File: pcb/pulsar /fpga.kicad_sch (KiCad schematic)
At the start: 0 parts

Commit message: feat(pcb): FPGA A1 schematic complete — MGT, ADC0-7 pinout, MUX sel
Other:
- added sheet A1 (MGT, clock) (fpga_a1.kicad_sch)
- added sheet B2 (IO bank 1) (fpga_b2.kicad_sch)
- added sheet C3 (IO bank 2) (fpga_c3.kicad_sch)
- added sheet D4 (IO bank 3) (fpga_d4.kicad_sch .kicad_sch)
- added sheet E5 (power + config) (fpga_e5.kicad_sch)
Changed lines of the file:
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@@
 	(generator_version "10.0")
 	(paper "A4")
+	(sheet
+		(at 114.3 73.66)
+		(size 90.17 40.64)
+		(exclude_from_sim no)
+		(in_bom yes)
+		(on_board yes)
+		(dnp no)
+		(fields_autoplaced yes)
+		(stroke
+			(width 0.1524)
+			(type solid)
+		)
+		(fill
+			(color 0 0 0 0)
+		)
+		(property "Sheetname" "D4 (IO bank 3)"
+			(at 114.3 72.9484 0)
+			(show_name no)
+			(do_not_autoplace no)
+			(effects
+				(font
+					(size 1.27 1.27)
+				)
+				(justify left bottom)
+			)
+		)
+		(property "Sheetfile" "fpga_d4.kicad_sch .kicad_sch"
+			(at 114.3 114.8846 0)
+			(show_name no)
+			(do_not_autoplace no)
+			(effects
+				(font
+					(size 1.27 1.27)
+				)
+				(justify left top)
+			)
+		)
+		(instances
+			(project "pulsar "
+				(path "/60c284f0-e6d7-47fc-9b46-38b478ecbf26/80956d0d-0521-4a41-bffb-11a8f02bc21e"
+					(page "11")
+				)
+			)
+		)
+	)
+	(sheet
+		(at 26.67 73.66)
+		(size 80.01 40.64)
+		(exclude_from_sim no)
+		(in_bom yes)
+		(on_board yes)
+		(dnp no)
+		(fields_autoplaced yes)
+		(stroke
+			(width 0.1524)
+			(type solid)
+		)
+		(fill
+			(color 0 0 0 0)
+		)
+		(property "Sheetname" "C3 (IO bank 2)"
+			(at 26.67 72.9484 0)
+			(show_name no)
+			(do_not_autoplace no)
+			(effects
+				(font
+					(size 1.27 1.27)
+				)
+				(justify left bottom)
+			)
+		)
+		(property "Sheetfile" "fpga_c3.kicad_sch"
+			(at 26.67 114.8846 0)
+			(show_name no)
+			(do_not_autoplace no)
+			(effects
+				(font
+					(size 1.27 1.27)
+				)
+				(justify left top)
+			)
+		)
+		(instances
+			(project "pulsar "
+				(path "/60c284f0-e6d7-47fc-9b46-38b478ecbf26/80956d0d-0521-4a41-bffb-11a8f02bc21e"
+					(page "10")
+				)
+			)
+		)
+	)
+	(sheet
+		(at 26.67 123.19)
+		(size 80.01 43.18)
+		(exclude_from_sim no)
+		(in_bom yes)
+		(on_board yes)
+		(dnp no)
+		(fields_autoplaced yes)
+		(stroke
+			(width 0.1524)
+			(type solid)
+		)
+		(fill
+			(color 0 0 0 0)
+		)
+		(property "Sheetname" "E5 (power + config)"
+			(at 26.67 122.4784 0)
+			(show_name no)
+			(do_not_autoplace no)
+			(effects
+				(font
+					(size 1.27 1.27)
+				)
+				(justify left bottom)
+			)
+		)
+		(property "Sheetfile" "fpga_e5.kicad_sch"
+			(at 26.67 166.9546 0)
+			(show_name no)
+			(do_not_autoplace no)
+			(effects
+				(font
+					(size 1.27 1.27)
+				)
+				(justify left top)
+			)
+		)
+		(instances
+			(project "pulsar "
+				(path "/60c284f0-e6d7-47fc-9b46-38b478ecbf26/80956d0d-0521-4a41-bffb-11a8f02bc21e"
+					(page "12")
+				)
+			)
+		)
+	)
+	(sheet
+		(at 114.3 21.59)
+		(size 90.17 46.99)
+		(exclude_from_sim no)
+		(in_bom yes)
+		(on_board yes)
+		(dnp no)
+		(fields_autoplaced yes)
+		(stroke
+			(width 0.1524)
+			(type solid)
+		)
+		(fill
+			(color 0 0 0 0)
+		)
+		(property "Sheetname" "B2 (IO bank 1)"
+			(at 114.3 20.8784 0)
+			(show_name no)
+			(do_not_autoplace no)
+			(effects
+				(font
+					(size 1.27 1.27)
+				)
+				(justify left bottom)
+			)
+		)
+		(property "Sheetfile" "fpga_b2.kicad_sch"
+			(at 114.3 69.1646 0)
+			(show_name no)
+			(do_not_autoplace no)
+			(effects
+				(font
+					(size 1.27 1.27)
+				)
+				(justify left top)
+			)
+		)
+		(instances
+			(project "pulsar "
+				(path "/60c284f0-e6d7-47fc-9b46-38b478ecbf26/80956d0d-0521-4a41-bffb-11a8f02bc21e"
+					(page "9")
+				)
+			)
+		)
+	)
+	(sheet
+		(at 26.67 21.59)
+		(size 80.01 46.99)
+		(exclude_from_sim no)
+		(in_bom yes)
+		(on_board yes)
+		(dnp no)
+		(fields_autoplaced yes)
+		(stroke
+			(width 0.1524)
+			(type solid)
+		)
+		(fill
+			(color 0 0 0 0)
+		)
+		(property "Sheetname" "A1 (MGT, clock)"
+			(at 26.67 20.8784 0)
+			(show_name no)
+			(do_not_autoplace no)
+			(effects
+				(font
+					(size 1.27 1.27)
+				)
+				(justify left bottom)
+			)
+		)
+		(property "Sheetfile" "fpga_a1.kicad_sch"
+			(at 26.67 69.1646 0)
+			(show_name no)
+			(do_not_autoplace no)
+			(effects
+				(font
+					(size 1.27 1.27)
+				)
+				(justify left top)
+			)
+		)
+		(instances
+			(project "pulsar "
+				(path "/60c284f0-e6d7-47fc-9b46-38b478ecbf26/80956d0d-0521-4a41-bffb-11a8f02bc21e"
+					(page "8")
+				)
+			)
+		)
+	)
 )

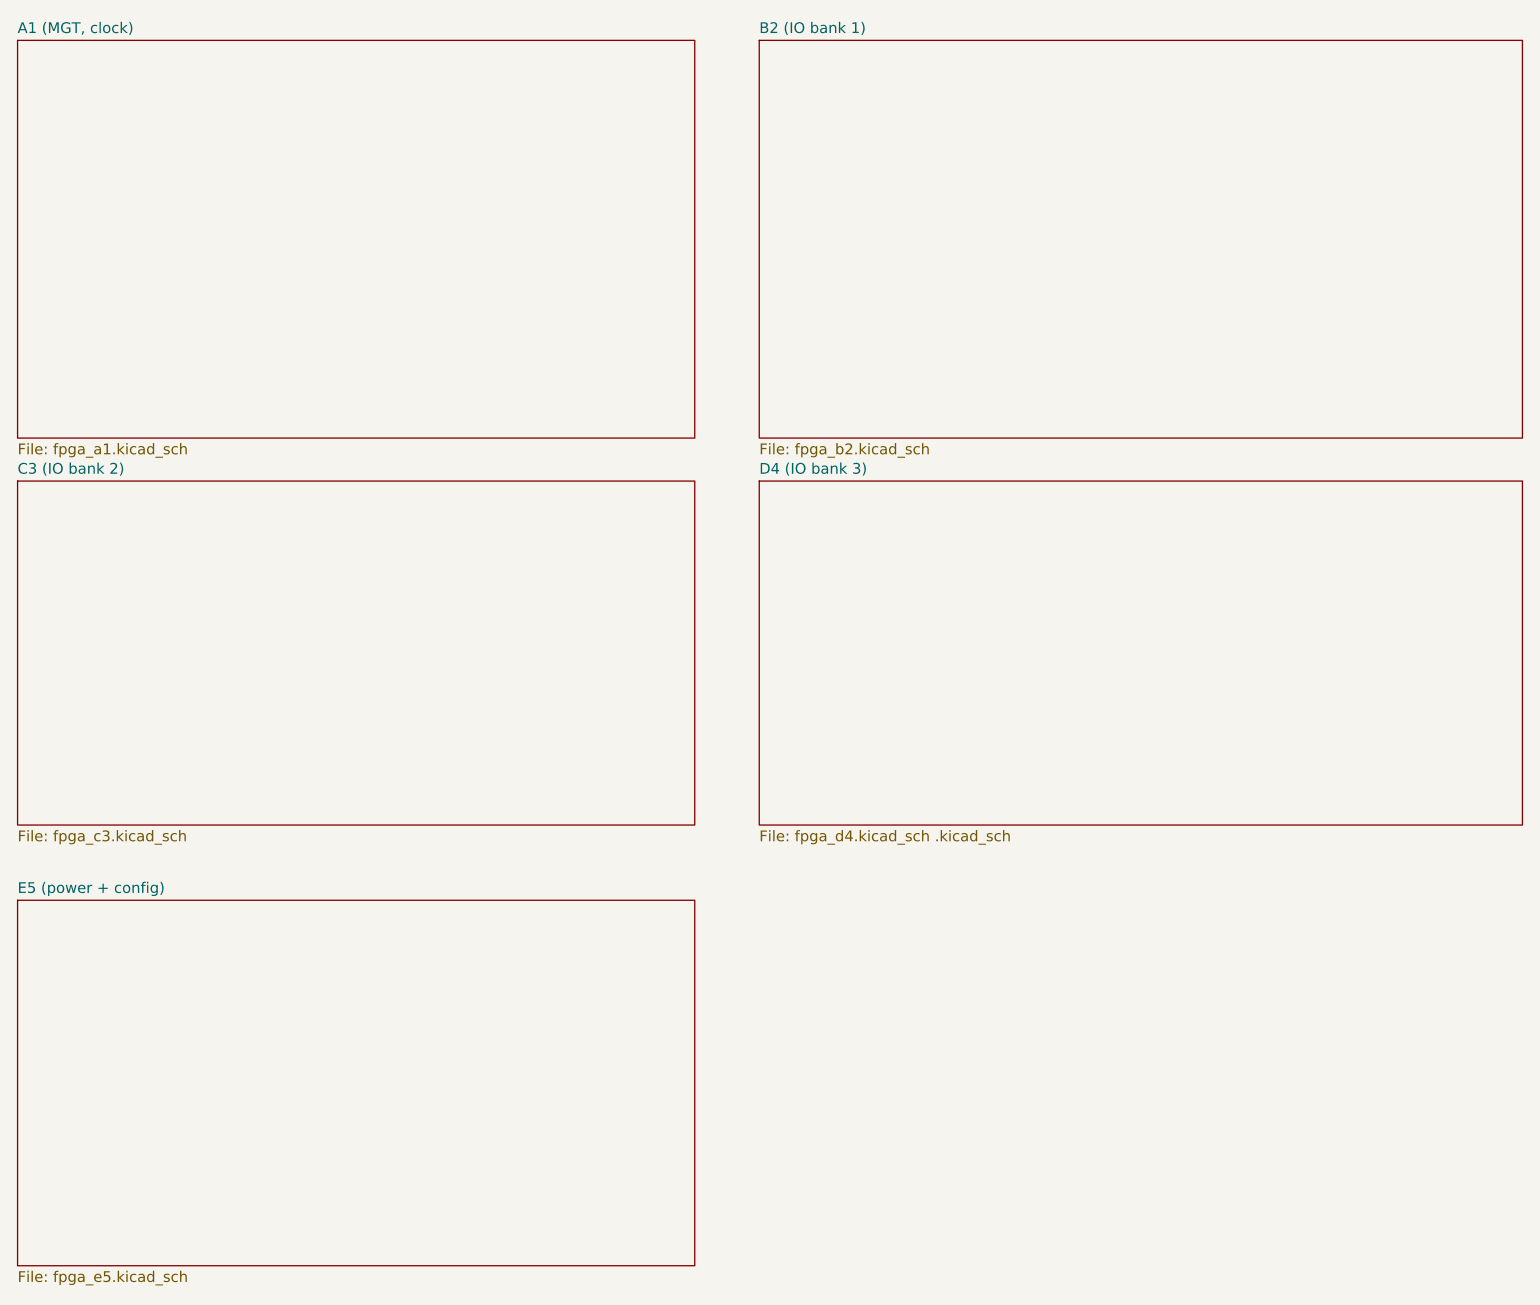
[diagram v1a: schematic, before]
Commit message: feat(pcb): FPGA schematic structure — full pinout A1, hierarchy reorganized
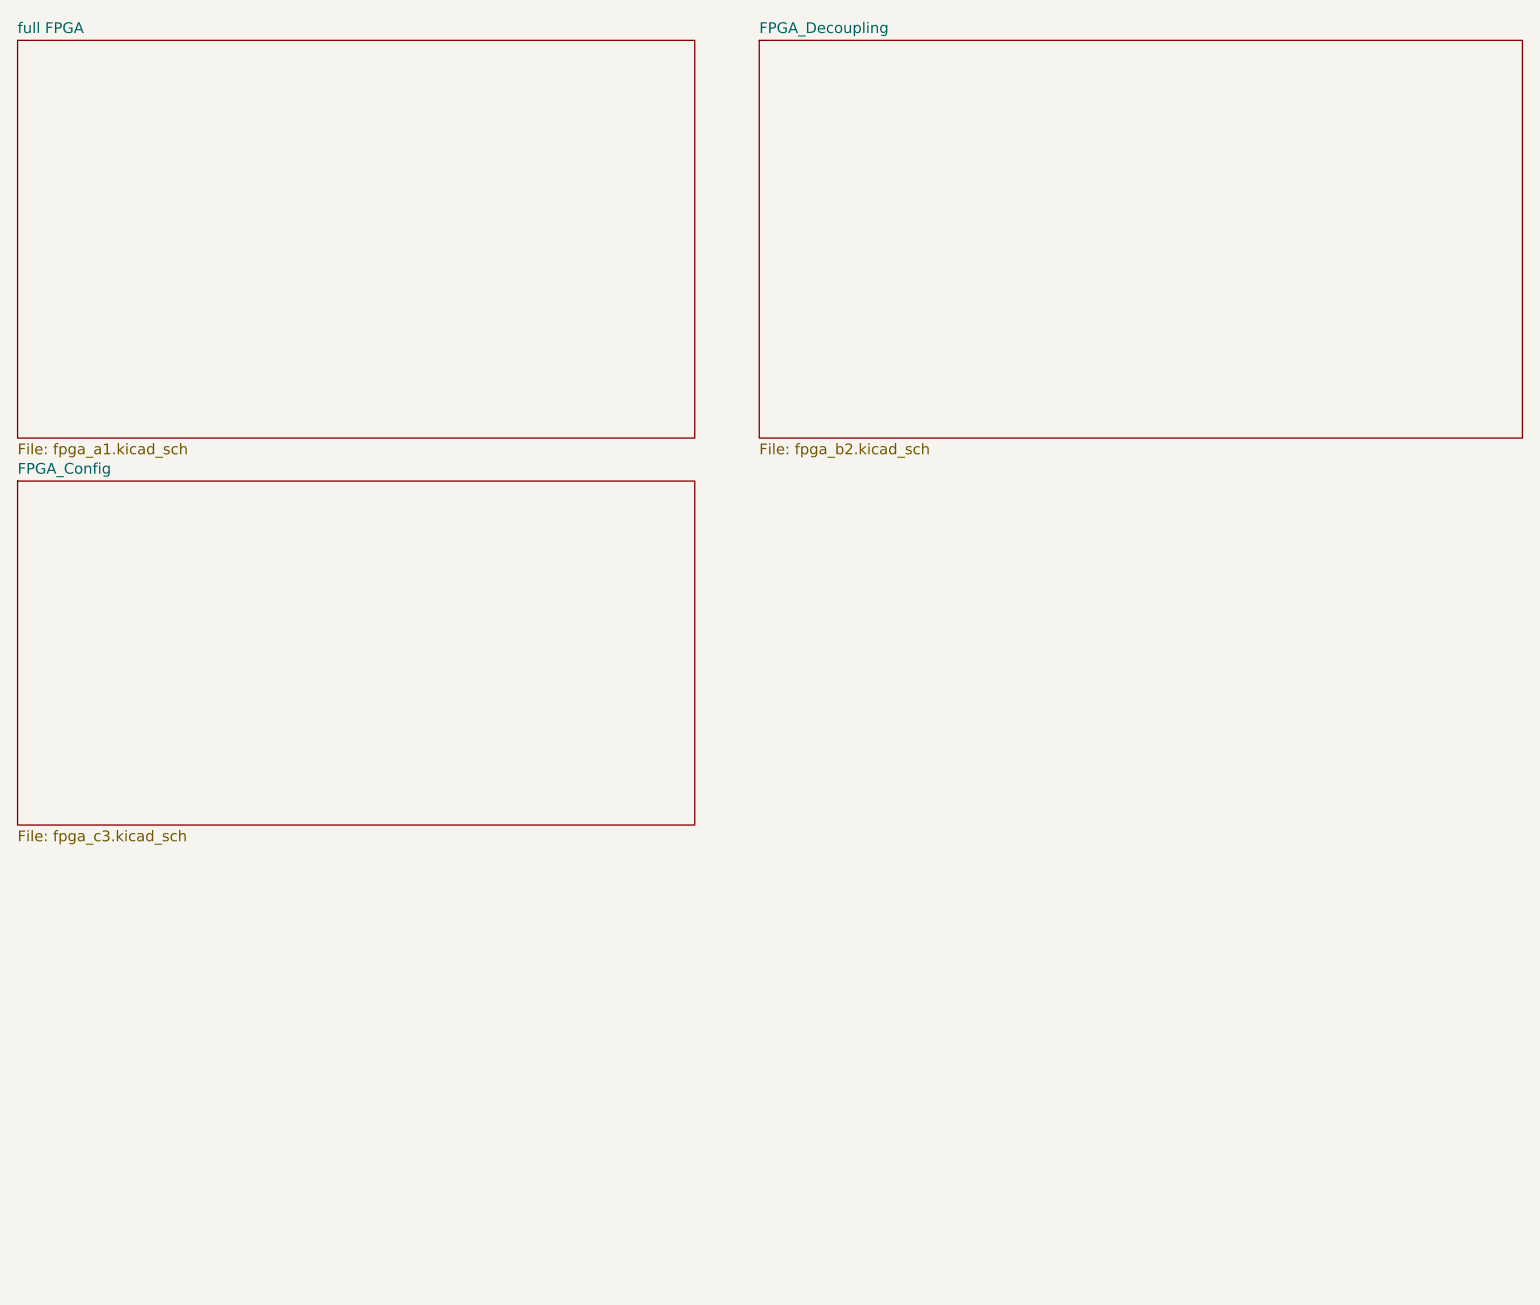
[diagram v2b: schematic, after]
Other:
- sheet A1 (MGT, clock) renamed full FPGA
- sheet B2 (IO bank 1) renamed FPGA_Decoupling
- sheet C3 (IO bank 2) renamed FPGA_Config
- removed sheet D4 (IO bank 3)
- removed sheet E5 (power + config)
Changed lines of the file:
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@@
 	(paper "A4")
-	(sheet
-		(at 114.3 73.66)
-		(size 90.17 40.64)
-		(exclude_from_sim no)
-		(in_bom yes)
-		(on_board yes)
-		(dnp no)
-		(fields_autoplaced yes)
-		(stroke
-			(width 0.1524)
-			(type solid)
-		)
-		(fill
-			(color 0 0 0 0)
-		)
-		(property "Sheetname" "D4 (IO bank 3)"
-			(at 114.3 72.9484 0)
-			(show_name no)
-			(do_not_autoplace no)
-			(effects
-				(font
-					(size 1.27 1.27)
-				)
-				(justify left bottom)
-			)
-		)
-		(property "Sheetfile" "fpga_d4.kicad_sch .kicad_sch"
-			(at 114.3 114.8846 0)
-			(show_name no)
-			(do_not_autoplace no)
-			(effects
-				(font
-					(size 1.27 1.27)
-				)
-				(justify left top)
-			)
-		)
-		(instances
-			(project "pulsar "
-				(path "/60c284f0-e6d7-47fc-9b46-38b478ecbf26/80956d0d-0521-4a41-bffb-11a8f02bc21e"
-					(page "11")
-				)
-			)
-		)
-	)
 	(sheet
 		(at 26.67 73.66)
@@
 			(color 0 0 0 0)
 		)
-		(property "Sheetname" "C3 (IO bank 2)"
+		(property "Sheetname" "FPGA_Config"
 			(at 26.67 72.9484 0)
 			(show_name no)
@@
 	)
 	(sheet
-		(at 26.67 123.19)
-		(size 80.01 43.18)
-		(exclude_from_sim no)
-		(in_bom yes)
-		(on_board yes)
-		(dnp no)
-		(fields_autoplaced yes)
-		(stroke
-			(width 0.1524)
-			(type solid)
-		)
-		(fill
-			(color 0 0 0 0)
-		)
-		(property "Sheetname" "E5 (power + config)"
-			(at 26.67 122.4784 0)
-			(show_name no)
-			(do_not_autoplace no)
-			(effects
-				(font
-					(size 1.27 1.27)
-				)
-				(justify left bottom)
-			)
-		)
-		(property "Sheetfile" "fpga_e5.kicad_sch"
-			(at 26.67 166.9546 0)
-			(show_name no)
-			(do_not_autoplace no)
-			(effects
-				(font
-					(size 1.27 1.27)
-				)
-				(justify left top)
-			)
-		)
-		(instances
-			(project "pulsar "
-				(path "/60c284f0-e6d7-47fc-9b46-38b478ecbf26/80956d0d-0521-4a41-bffb-11a8f02bc21e"
-					(page "12")
-				)
-			)
-		)
-	)
-	(sheet
 		(at 114.3 21.59)
 		(size 90.17 46.99)
@@
 			(color 0 0 0 0)
 		)
-		(property "Sheetname" "B2 (IO bank 1)"
+		(property "Sheetname" "FPGA_Decoupling"
 			(at 114.3 20.8784 0)
 			(show_name no)
@@
 			(color 0 0 0 0)
 		)
-		(property "Sheetname" "A1 (MGT, clock)"
+		(property "Sheetname" "full FPGA"
 			(at 26.67 20.8784 0)
 			(show_name no)
